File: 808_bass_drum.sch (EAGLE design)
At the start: 56 parts, among them IC1 TL072P, Q1 bc546, Q2 bc556, Q3 bc546, Q4 bc546, Q5 bc546, Q6 bc546

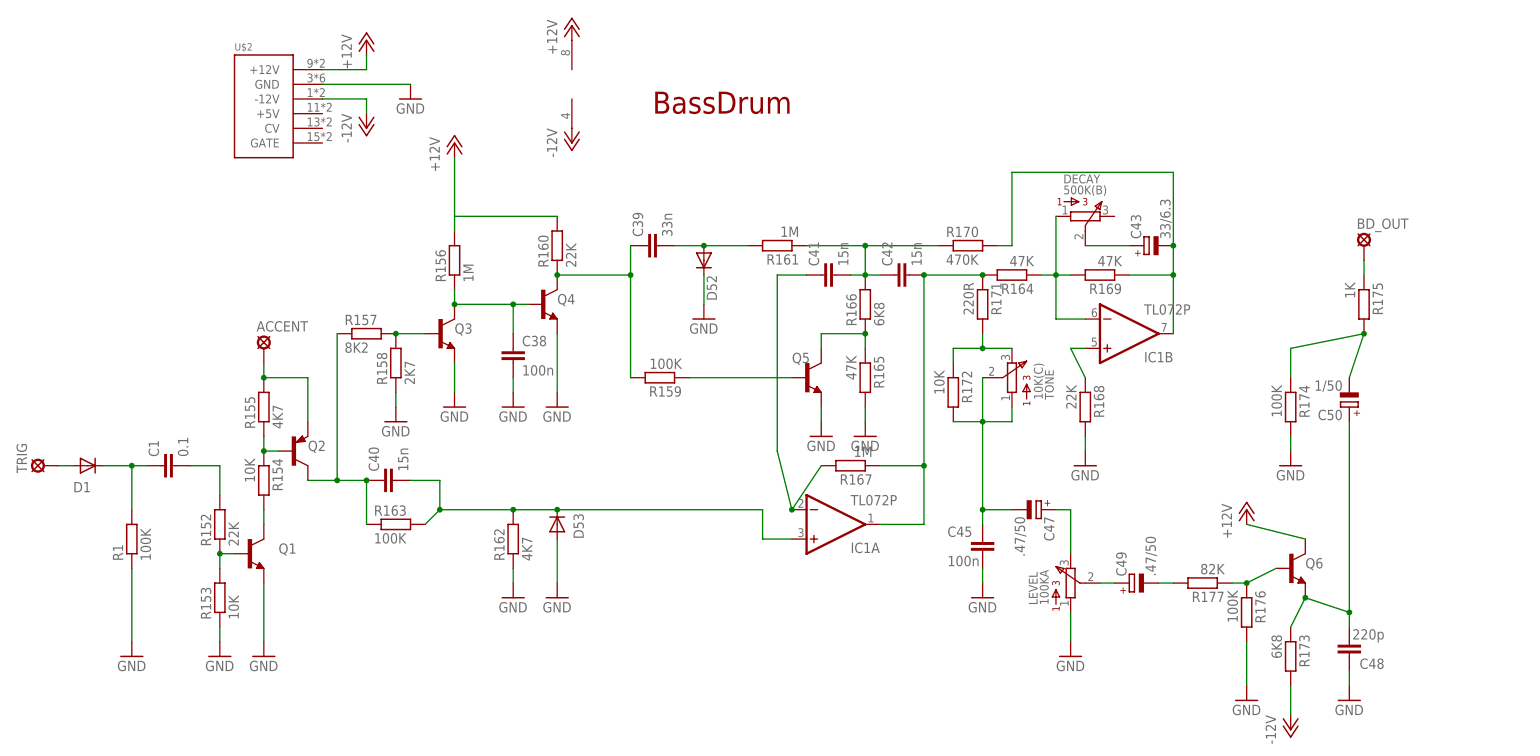
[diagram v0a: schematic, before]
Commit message: updating parts and conventions
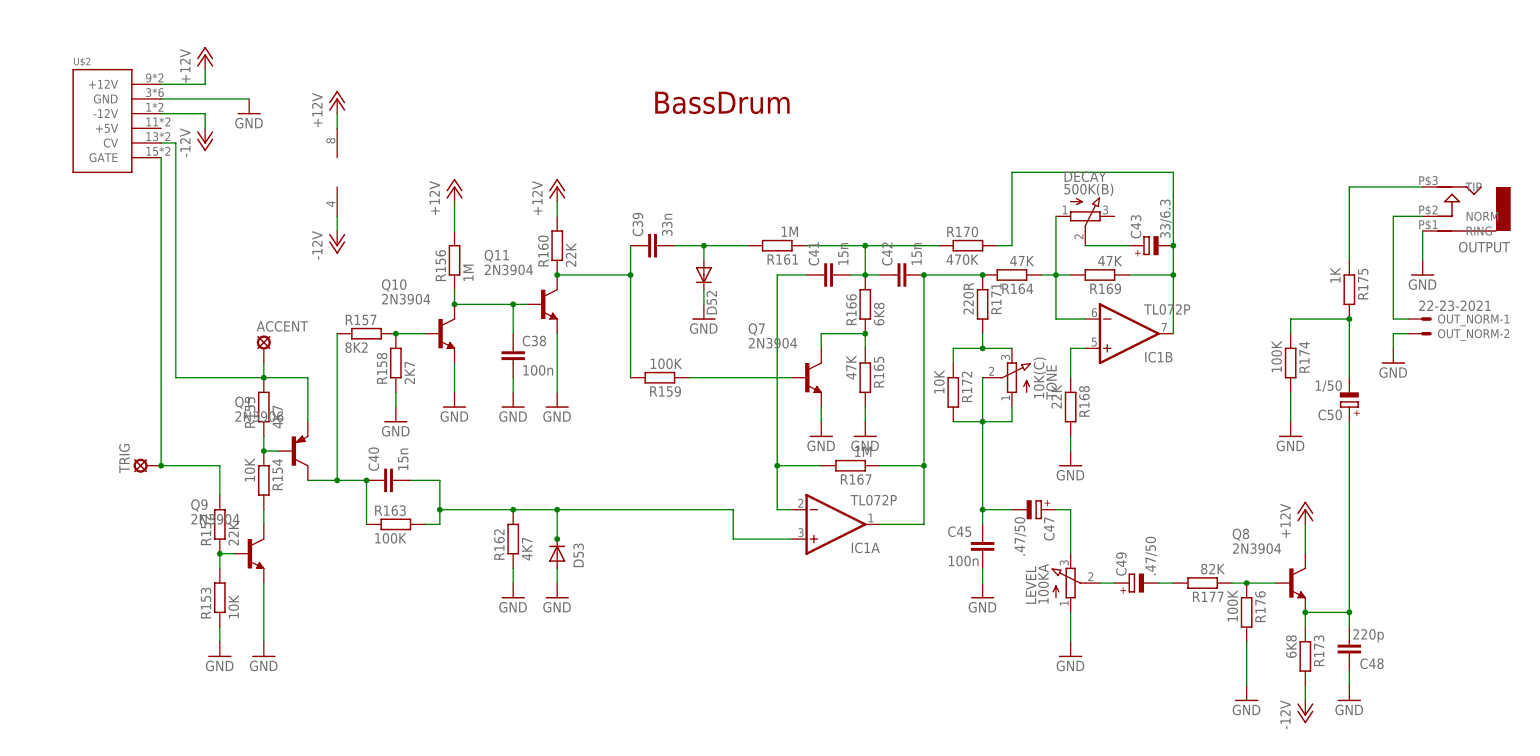
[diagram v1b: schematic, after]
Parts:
- removed BD_OUT: LSP10, solpad:LSP10
- removed C1: 0.1, TR808clone:C-EU050-024X044
- removed D1: 1N4148DO35-7, TR808clone:1N4148DO35-7
- removed Q2: bc556, transistor:BC556A-PNP-TO92-EBC
- removed Q3, Q4, Q5, Q6: bc546, transistor:BC546-NPN-TO92-CBE
- removed R1: 100K, TR808clone:R-EU_0207/5V
- added OUTPUT: AUDIO-JACK, erthenvar:AUDIO-JACK
- added OUT_NORM: 22-23-2021, con-molex:22-23-2021
- added Q10, Q11, Q7, Q8, Q9: 2N3904, 808_lt:2N3904
- DECAY, LEVEL, TONE: device bourns:91 -> pot:3RP/1610N
- Q1: value bc546 -> 2N3906; device transistor:BC546-NPN-TO92-CBE -> 808_lt:2N3906
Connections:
- removed net N$3 (its old number): BD_OUT.MP, R175.1
- removed net N$5: C1.1, D1.C, R1.2
- removed net N$6: C1.2, R152.2
- new net LT_LC_OUT: OUTPUT.TIP, R175.1
- new net N$7: OUTPUT.NORM, OUT_NORM-1.S
- net +12V: now also Q8.C; no longer Q6.C
- net GND: now also LEVEL.A, OUTPUT.RING, OUT_NORM-2.S, Q10.E, Q11.E, Q7.E, Q9.E; no longer LEVEL.1, Q1.E, Q3.E, Q4.E, Q5.E, R1.1
- net N$1: now also DECAY.A; no longer DECAY.1
- net N$162: now also Q10.C, Q11.B; no longer Q3.C, Q4.B
- net N$164: now also Q1.B; no longer Q2.B
- net N$168: now also Q7.C; no longer Q5.C
- net N$169: now also Q10.B; no longer Q3.B
- net N$188: now also Q9.C; no longer Q1.C
- net N$190: now also Q11.C; no longer Q4.C
- net N$191: now also Q1.C; no longer Q2.C
- net N$193: now also Q7.B; no longer Q5.B
- net N$198: now also TONE.A, TONE.S; no longer TONE.1, TONE.2
- net N$199: now also TONE.E; no longer TONE.3
- net N$203: now also Q8.B; no longer Q6.B
- net N$204: now also Q8.E; no longer Q6.E
- net N$206: now also LEVEL.E; no longer LEVEL.3
- net N$207: now also LEVEL.S; no longer LEVEL.2
- net N$208: now also DECAY.S; no longer DECAY.2
- net N$217: now also Q9.B; no longer Q1.B
- net N$4: now also R152.2, U$2.GATE; no longer D1.A
- net TRIG: now also Q1.E, U$2.CV; no longer Q2.E
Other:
- moved on the sheet: D52, D53, R168, R173, R174, R175, TRIG, U$2
